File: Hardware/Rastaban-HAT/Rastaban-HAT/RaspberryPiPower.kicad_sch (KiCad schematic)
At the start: 19 parts, among them IC2 DMMT5401-7-F, Q3 DMG2305UX-7, U5 RT7272AGSP

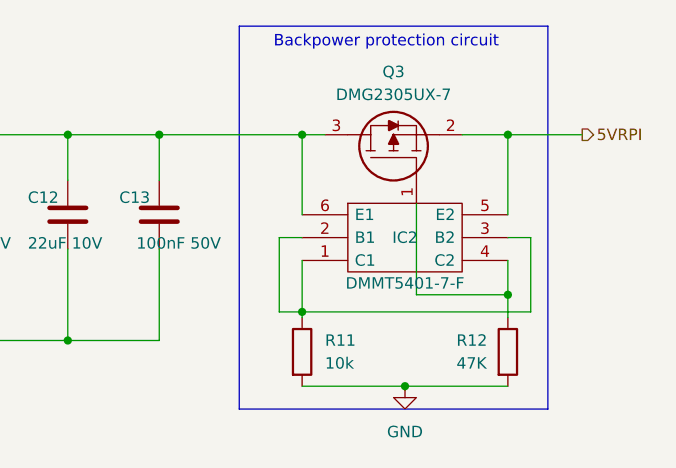
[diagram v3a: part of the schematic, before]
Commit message: Started changing capacitor types and sizes
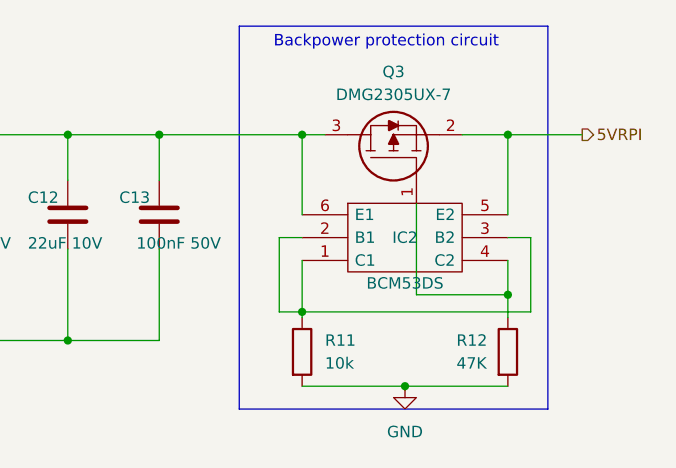
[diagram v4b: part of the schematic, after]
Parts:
- C11, C12: footprint Capacitor_SMD:CP_Elec_6.3x7.7 -> Capacitor_SMD:CP_Elec_3x5.4
- C13, C8: footprint Capacitor_SMD:CP_Elec_4x5.4 -> Capacitor_SMD:C_0805_2012Metric_Pad1.18x1.45mm_HandSolder
- IC2: value DMMT5401-7-F -> BCM53DS; Height 1.4 -> (none); Manufacturer_Name Diodes Inc. -> (none); Manufacturer_Part_Number DMMT5401-7-F -> (none); Mouser Part Number 621-DMMT5401-7-F -> 771-BCM53DSFs; Mouser Price/Stock https://www.mouser.co.uk/ProductDetail/Diodes-Incorporated/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 -> (none)
- Q3: Height 1.1 -> (none); LCSC (none) -> C2940629; Manufacturer_Name Diodes Inc. -> (none); Manufacturer_Part_Number DMG2305UX-7 -> (none); Mouser Part Number 621-DMG2305UX-7 -> (none); Mouser Price/Stock https://www.mouser.co.uk/ProductDetail/Diodes-Incorporated/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 -> (none)
- U5: LCSC (none) -> C3031672; MANUFACTURER Richtek USA Inc. -> (none); MAXIMUM_PACKAGE_HEIGHT 1.753 mm -> (none); PARTREV June 2015 -> (none); Purpose (none) -> StepDown converter; STANDARD IPC-7351B -> (none)
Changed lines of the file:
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@@
       (effects (font (size 1.27 1.27)) (justify left) hide)
     )
-    (property "Height" "1.1" (id 5) (at 244.475 90.17 0)
-      (effects (font (size 1.27 1.27)) (justify left) hide)
-    )
-    (property "Mouser Part Number" "621-DMG2305UX-7" (id 6) (at 247.015 90.17 0)
-      (effects (font (size 1.27 1.27)) (justify left) hide)
-    )
-    (property "Mouser Price/Stock" "https://www.mouser.co.uk/ProductDetail/Diodes-Incorporated/DMG2305UX-7?qs=L1DZKBg7t5F%2FNBHrjfxC%252Bg%3D%3D" (id 7) (at 249.555 90.17 0)
-      (effects (font (size 1.27 1.27)) (justify left) hide)
-    )
-    (property "Manufacturer_Name" "Diodes Inc." (id 8) (at 252.095 90.17 0)
-      (effects (font (size 1.27 1.27)) (justify left) hide)
-    )
-    (property "Manufacturer_Part_Number" "DMG2305UX-7" (id 9) (at 254.635 90.17 0)
-      (effects (font (size 1.27 1.27)) (justify left) hide)
+    (property "LCSC" "C2940629" (id 6) (at 235.585 101.6 90)
+      (effects (font (size 1.27 1.27)) hide)
     )
     (pin "1")
@@
       (effects (font (size 1.27 1.27)) (justify right))
     )
-    (property "Footprint" "Capacitor_SMD:CP_Elec_6.3x7.7" (id 2) (at 185.7248 99.06 0)
+    (property "Footprint" "Capacitor_SMD:CP_Elec_3x5.4" (id 2) (at 185.7248 99.06 0)
       (effects (font (size 1.27 1.27)) hide)
     )
@@
       (effects (font (size 1.27 1.27)) (justify right))
     )
-    (property "Footprint" "Capacitor_SMD:CP_Elec_4x5.4" (id 2) (at 206.0448 99.06 0)
+    (property "Footprint" "Capacitor_SMD:C_0805_2012Metric_Pad1.18x1.45mm_HandSolder" (id 2) (at 206.0448 99.06 0)
       (effects (font (size 1.27 1.27)) hide)
     )
@@
       (effects (font (size 1.27 1.27)) (justify left bottom) hide)
     )
-    (property "Datasheet" "" (id 3) (at 139.7 101.6 0)
+    (property "Datasheet" "https://datasheet.lcsc.com/lcsc/2206101730_Richtek-Tech-RT7272AGSP_C3031672.pdf" (id 3) (at 139.7 101.6 0)
       (effects (font (size 1.27 1.27)) (justify left bottom) hide)
     )
-    (property "MAXIMUM_PACKAGE_HEIGHT" "1.753 mm" (id 4) (at 133.35 118.11 0)
-      (effects (font (size 1.27 1.27)) (justify left bottom) hide)
-    )
-    (property "STANDARD" "IPC-7351B" (id 5) (at 134.62 120.65 0)
-      (effects (font (size 1.27 1.27)) (justify left bottom) hide)
-    )
-    (property "PARTREV" "June 2015" (id 6) (at 132.08 115.57 0)
-      (effects (font (size 1.27 1.27)) (justify left bottom) hide)
-    )
-    (property "MANUFACTURER" "Richtek USA Inc." (id 7) (at 129.54 113.03 0)
-      (effects (font (size 1.27 1.27)) (justify left bottom) hide)
+    (property "Purpose" "StepDown converter" (id 4) (at 135.89 101.6 0)
+      (effects (font (size 1.27 1.27)) hide)
+    )
+    (property "LCSC" "C3031672" (id 5) (at 135.89 101.6 0)
+      (effects (font (size 1.27 1.27)) hide)
     )
     (pin "1")
@@
     (in_bom yes) (on_board yes)
     (property "Reference" "IC2" (id 0) (at 234.315 105.41 0))
-    (property "Value" "DMMT5401-7-F" (id 1) (at 234.315 110.49 0))
+    (property "Value" "BCM53DS" (id 1) (at 234.315 110.49 0))
     (property "Footprint" "SamacSys_Parts:SOT95P285X140-6N" (id 2) (at 241.935 100.33 0)
       (effects (font (size 1.27 1.27)) (justify left) hide)
     )
-    (property "Datasheet" "https://datasheet.datasheetarchive.com/originals/distributors/Datasheets-9/DSA-164366.pdf" (id 3) (at 241.935 102.87 0)
-      (effects (font (size 1.27 1.27)) (justify left) hide)
-    )
-    (property "Description" "Transistor Dual PNP 150V 0.2A SOT26-6 Diodes Inc DMMT5401-7-F Dual PNP Bipolar Transistor, -200 mA, -150 V, 6-Pin SOT-26" (id 4) (at 241.935 105.41 0)
-      (effects (font (size 1.27 1.27)) (justify left) hide)
-    )
-    (property "Height" "1.4" (id 5) (at 241.935 107.95 0)
-      (effects (font (size 1.27 1.27)) (justify left) hide)
-    )
-    (property "Mouser Part Number" "621-DMMT5401-7-F" (id 6) (at 241.935 110.49 0)
-      (effects (font (size 1.27 1.27)) (justify left) hide)
-    )
-    (property "Mouser Price/Stock" "https://www.mouser.co.uk/ProductDetail/Diodes-Incorporated/DMMT5401-7-F?qs=hiZRsJxw0h3f7LzTPwvEFQ%3D%3D" (id 7) (at 241.935 113.03 0)
-      (effects (font (size 1.27 1.27)) (justify left) hide)
-    )
-    (property "Manufacturer_Name" "Diodes Inc." (id 8) (at 241.935 115.57 0)
-      (effects (font (size 1.27 1.27)) (justify left) hide)
-    )
-    (property "Manufacturer_Part_Number" "DMMT5401-7-F" (id 9) (at 241.935 118.11 0)
+    (property "Datasheet" "https://nl.mouser.com/datasheet/2/916/BCM53DS-1370670.pdf" (id 3) (at 241.935 102.87 0)
+      (effects (font (size 1.27 1.27)) (justify left) hide)
+    )
+    (property "Description" "80 V, 1 A PNP/PNP matched double transistors" (id 4) (at 241.935 105.41 0)
+      (effects (font (size 1.27 1.27)) (justify left) hide)
+    )
+    (property "Mouser Part Number" "771-BCM53DSFs" (id 6) (at 241.935 110.49 0)
       (effects (font (size 1.27 1.27)) (justify left) hide)
     )
@@
       (effects (font (size 1.27 1.27)) (justify right))
     )
-    (property "Footprint" "Capacitor_SMD:CP_Elec_6.3x7.7" (id 2) (at 195.8848 99.06 0)
+    (property "Footprint" "Capacitor_SMD:CP_Elec_3x5.4" (id 2) (at 195.8848 99.06 0)
       (effects (font (size 1.27 1.27)) hide)
     )
@@
       (effects (font (size 1.27 1.27)) (justify left))
     )
-    (property "Footprint" "Capacitor_SMD:CP_Elec_4x5.4" (id 2) (at 113.9952 104.14 0)
-      (effects (font (size 1.27 1.27)) hide)
-    )
+    (property "Footprint" "Capacitor_SMD:C_0805_2012Metric_Pad1.18x1.45mm_HandSolder" (id 2) (at 113.9952 104.14 0)
+      (effects (font (size 1.27 1.27)) hide)
+    )

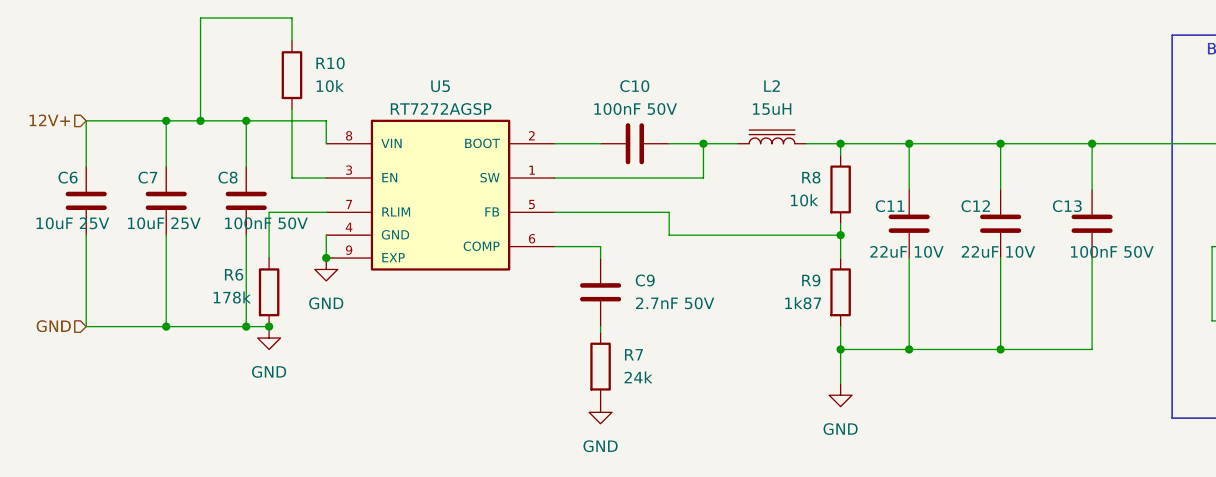
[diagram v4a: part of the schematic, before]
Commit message: changed all capacitor voltages to 50V
This makes ordering and component selection easier.
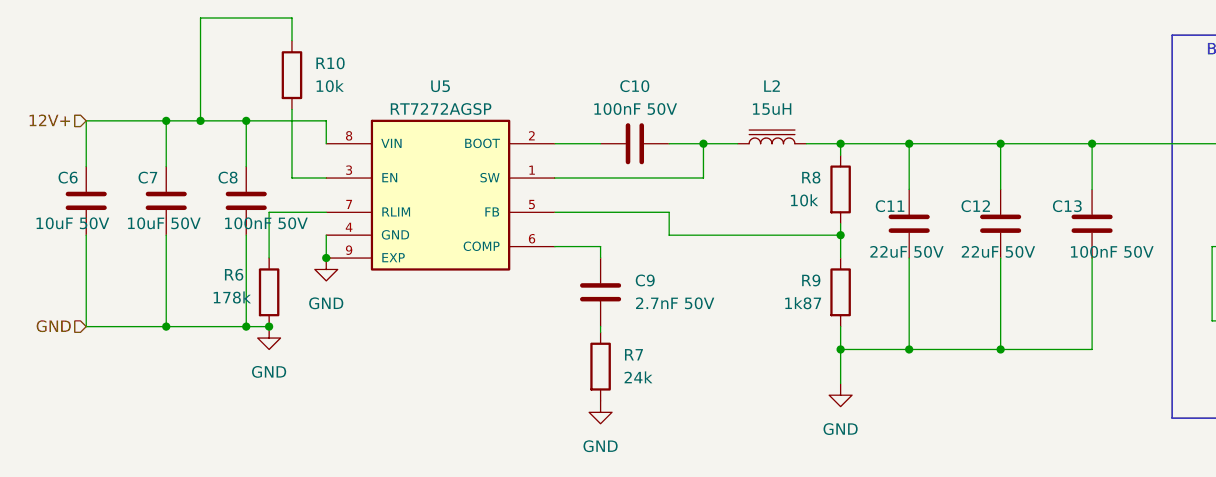
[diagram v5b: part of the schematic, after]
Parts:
- C11, C12: value 22uF 10V -> 22uF 50V
- C6, C7: value 10uF 25V -> 10uF 50V
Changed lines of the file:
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@@
       (effects (font (size 1.27 1.27)) (justify right))
     )
-    (property "Value" "22uF 10V" (id 1) (at 182.245 106.045 0)
+    (property "Value" "22uF 50V" (id 1) (at 182.245 106.045 0)
       (effects (font (size 1.27 1.27)) (justify right))
     )
@@
       (effects (font (size 1.27 1.27)) (justify left))
     )
-    (property "Value" "10uF 25V" (id 1) (at 89.535 102.87 0)
+    (property "Value" "10uF 50V" (id 1) (at 89.535 102.87 0)
       (effects (font (size 1.27 1.27)) (justify left))
     )
@@
       (effects (font (size 1.27 1.27)) (justify left))
     )
-    (property "Value" "10uF 25V" (id 1) (at 99.695 102.87 0)
+    (property "Value" "10uF 50V" (id 1) (at 99.695 102.87 0)
       (effects (font (size 1.27 1.27)) (justify left))
     )
@@
       (effects (font (size 1.27 1.27)) (justify right))
     )
-    (property "Value" "22uF 10V" (id 1) (at 192.405 106.045 0)
+    (property "Value" "22uF 50V" (id 1) (at 192.405 106.045 0)
       (effects (font (size 1.27 1.27)) (justify right))
     )

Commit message: finished BOM file
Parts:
- C10, C13, C8: LCSC (none) -> C531179
- C11, C12: footprint Capacitor_SMD:CP_Elec_3x5.4 -> Capacitor_SMD:CP_Elec_6.3x5.8; LCSC (none) -> C128458
- C6, C7: footprint Capacitor_SMD:CP_Elec_3x5.4 -> Capacitor_SMD:C_0805_2012Metric_Pad1.18x1.45mm_HandSolder; LCSC (none) -> C17024
- C9: LCSC (none) -> C376966
- IC2: Mouser (none) -> 771-BCM53DSF
- L2: LCSC (none) -> CY54-15UH
- Q3: Mouser (none) -> 621-DMG2305UX-7
- R10, R11, R8: LCSC (none) -> C5140188
- R12: LCSC (none) -> C102018
- R6: LCSC (none) -> C218368
- R7: LCSC (none) -> C2907246
- R9: Mouser (none) -> 279-CPF0805B1K87E1
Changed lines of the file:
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@@
+      (effects (font (size 1.27 1.27)) hide)
+    )
+    (property "LCSC" "C102018" (id 4) (at 245.745 118.11 0)
       (effects (font (size 1.27 1.27)) hide)
     )
@@
       (effects (font (size 1.27 1.27)) hide)
     )
+    (property "Mouser" "621-DMG2305UX-7" (id 7) (at 235.585 101.6 90)
+      (effects (font (size 1.27 1.27)) hide)
+    )
     (pin "1")
     (pin "2")
@@
       (effects (font (size 1.27 1.27)) hide)
     )
+    (property "LCSC" "C5140188" (id 4) (at 118.11 86.36 0)
+      (effects (font (size 1.27 1.27)) hide)
+    )
     (pin "1")
     (pin "2")
@@
       (effects (font (size 1.27 1.27)) hide)
     )
+    (property "LCSC" "C2907246" (id 4) (at 152.4 118.745 0)
+      (effects (font (size 1.27 1.27)) hide)
+    )
     (pin "1")
     (pin "2")
@@
       (effects (font (size 1.27 1.27)) hide)
     )
+    (property "LCSC" "C218368" (id 4) (at 115.57 110.49 0)
+      (effects (font (size 1.27 1.27)) hide)
+    )
     (pin "1")
     (pin "2")
@@
       (effects (font (size 1.27 1.27)) hide)
     )
+    (property "LCSC" "C5140188" (id 4) (at 222.885 118.11 0)
+      (effects (font (size 1.27 1.27)) hide)
+    )
     (pin "1")
     (pin "2")
@@
       (effects (font (size 1.27 1.27)) (justify right))
     )
-    (property "Footprint" "Capacitor_SMD:CP_Elec_3x5.4" (id 2) (at 185.7248 99.06 0)
+    (property "Footprint" "Capacitor_SMD:CP_Elec_6.3x5.8" (id 2) (at 185.7248 99.06 0)
       (effects (font (size 1.27 1.27)) hide)
     )
@@
       (effects (font (size 1.27 1.27)) hide)
     )
+    (property "LCSC" "C128458" (id 4) (at 186.69 102.87 0)
+      (effects (font (size 1.27 1.27)) hide)
+    )
     (pin "1")
     (pin "2")
@@
       (effects (font (size 1.27 1.27)) (justify left))
     )
-    (property "Footprint" "Capacitor_SMD:CP_Elec_3x5.4" (id 2) (at 96.2152 104.14 0)
+    (property "Footprint" "Capacitor_SMD:C_0805_2012Metric_Pad1.18x1.45mm_HandSolder" (id 2) (at 96.2152 104.14 0)
       (effects (font (size 1.27 1.27)) hide)
     )
     (property "Datasheet" "~" (id 3) (at 95.25 100.33 0)
+      (effects (font (size 1.27 1.27)) hide)
+    )
+    (property "LCSC" "C17024" (id 4) (at 95.25 100.33 0)
       (effects (font (size 1.27 1.27)) hide)
     )
@@
       (effects (font (size 1.27 1.27)) hide)
     )
+    (property "LCSC" "C531179" (id 4) (at 207.01 102.87 0)
+      (effects (font (size 1.27 1.27)) hide)
+    )
     (pin "1")
     (pin "2")
@@
       (effects (font (size 1.27 1.27)) (justify left))
     )
-    (property "Footprint" "Capacitor_SMD:CP_Elec_3x5.4" (id 2) (at 105.1052 104.14 0)
+    (property "Footprint" "Capacitor_SMD:C_0805_2012Metric_Pad1.18x1.45mm_HandSolder" (id 2) (at 105.1052 104.14 0)
       (effects (font (size 1.27 1.27)) hide)
     )
     (property "Datasheet" "~" (id 3) (at 104.14 100.33 0)
+      (effects (font (size 1.27 1.27)) hide)
+    )
+    (property "LCSC" "C17024" (id 4) (at 104.14 100.33 0)
       (effects (font (size 1.27 1.27)) hide)
     )
@@
       (effects (font (size 1.27 1.27)) hide)
     )
+    (property "LCSC" "C376966" (id 4) (at 152.4 110.49 0)
+      (effects (font (size 1.27 1.27)) hide)
+    )
     (pin "1")
     (pin "2")
@@
     )
     (property "Purpose" "Dual PNP small signal transistor" (id 10) (at 222.885 102.87 0)
+      (effects (font (size 1.27 1.27)) hide)
+    )
+    (property "Mouser" "771-BCM53DSF" (id 11) (at 222.885 102.87 0)
       (effects (font (size 1.27 1.27)) hide)
     )
@@
       (effects (font (size 1.27 1.27)) (justify right))
     )
-    (property "Footprint" "Capacitor_SMD:CP_Elec_3x5.4" (id 2) (at 195.8848 99.06 0)
+    (property "Footprint" "Capacitor_SMD:CP_Elec_6.3x5.8" (id 2) (at 195.8848 99.06 0)
       (effects (font (size 1.27 1.27)) hide)
     )
@@
       (effects (font (size 1.27 1.27)) hide)
     )
+    (property "LCSC" "C128458" (id 4) (at 196.85 102.87 0)
+      (effects (font (size 1.27 1.27)) hide)
+    )
     (pin "1")
     (pin "2")
@@
       (effects (font (size 1.27 1.27)) hide)
     )
+    (property "LCSC" "C5140188" (id 4) (at 179.07 99.06 0)
+      (effects (font (size 1.27 1.27)) hide)
+    )
     (pin "1")
     (pin "2")
@@
     )
     (property "Datasheet" "~" (id 3) (at 179.07 110.49 0)
+      (effects (font (size 1.27 1.27)) hide)
+    )
+    (property "Mouser" "279-CPF0805B1K87E1" (id 4) (at 179.07 110.49 0)
       (effects (font (size 1.27 1.27)) hide)
     )
@@
       (effects (font (size 1.27 1.27)) hide)
     )
+    (property "LCSC" "C531179" (id 4) (at 156.21 93.98 0)
+      (effects (font (size 1.27 1.27)) hide)
+    )
     (pin "1")
     (pin "2")
@@
     )
     (property "Datasheet" "~" (id 3) (at 113.03 100.33 0)
+      (effects (font (size 1.27 1.27)) hide)
+    )
+    (property "LCSC" "C531179" (id 4) (at 113.03 100.33 0)
       (effects (font (size 1.27 1.27)) hide)
     )
@@
       (effects (font (size 1.27 1.27)) hide)
     )
+    (property "LCSC" "CY54-15UH" (id 4) (at 171.45 93.98 0)
+      (effects (font (size 1.27 1.27)) hide)
+    )

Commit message: routing started again
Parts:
- IC2: footprint SamacSys_Parts:SOT95P285X140-6N -> SamacSys_Parts:SOT95P280X145-6N; Mouser Part Number 771-BCM53DSFs -> 771-BCM53DSF
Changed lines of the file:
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@@
     (property "Reference" "IC2" (id 0) (at 234.315 105.41 0))
     (property "Value" "BCM53DS" (id 1) (at 234.315 110.49 0))
-    (property "Footprint" "SamacSys_Parts:SOT95P285X140-6N" (id 2) (at 241.935 100.33 0)
+    (property "Footprint" "SamacSys_Parts:SOT95P280X145-6N" (id 2) (at 241.935 100.33 0)
       (effects (font (size 1.27 1.27)) (justify left) hide)
     )
@@
       (effects (font (size 1.27 1.27)) (justify left) hide)
     )
-    (property "Mouser Part Number" "771-BCM53DSFs" (id 6) (at 241.935 110.49 0)
+    (property "Mouser Part Number" "771-BCM53DSF" (id 6) (at 241.935 110.49 0)
       (effects (font (size 1.27 1.27)) (justify left) hide)
     )
